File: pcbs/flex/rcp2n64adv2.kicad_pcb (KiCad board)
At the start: 2 copper layers, 129.6 x 25 mm, 17 parts, among them J1 Conn_01x01, J2 Conn_01x01, J3 Conn_01x01, J3.1 Conn_01x01, J4 Conn_01x01, J5 Conn_01x01, J6 Conn_01x30, U1 74LVC1G17, X1 n64_rcp_vid_aud_out_no_3v3_con, X2 Conn_01x01

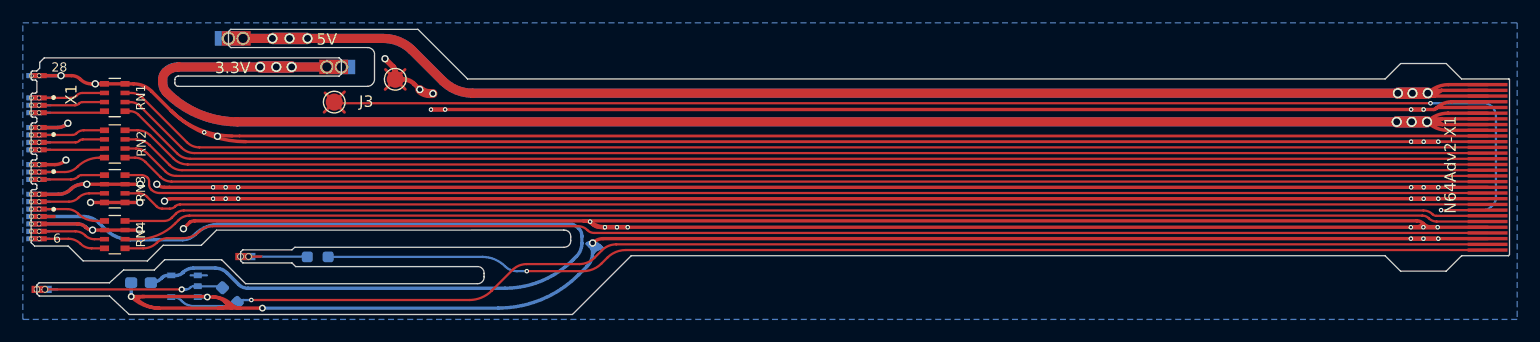
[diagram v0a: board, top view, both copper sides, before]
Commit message: update flex PCB with minor changes, e.g. added a logo
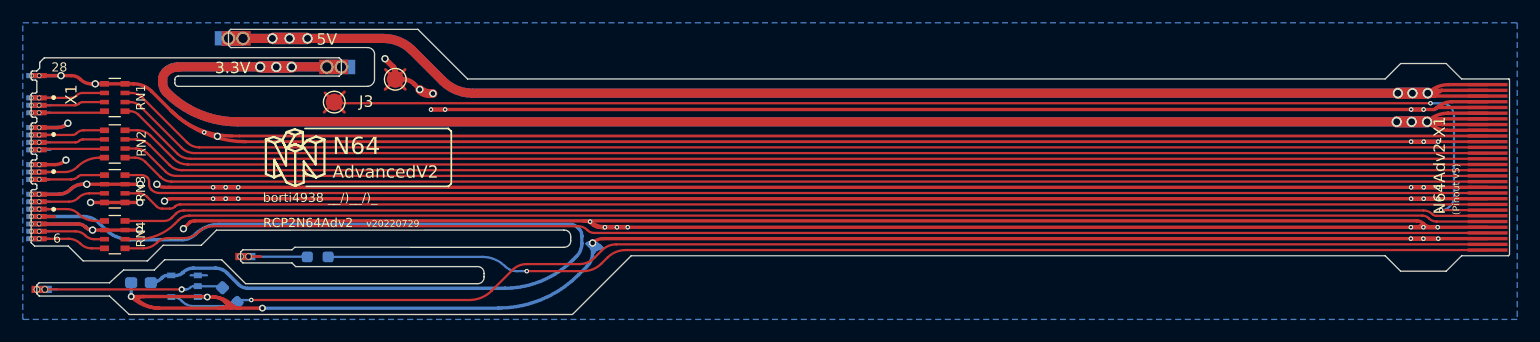
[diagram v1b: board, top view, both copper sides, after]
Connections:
- C1 pad 1: +3V3 -> VCC
- U1 pad 5: +3V3 -> VCC
- X2 pad 1: +3V3 -> VCC
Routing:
- net VCC: track 0.00 -> 91.3 mm
- net +3V3: track 381.2 -> 289.9 mm
- net Net-(J3-Pad1): track 124.1 -> 116.7 mm
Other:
- board text added: "(Pinout v5)"
- board text added: "(U1,C1) or R1"
- board text added: "AdvancedV2"
- board text added: "N64"
- board text added: "RCP2N64Adv2"
- board text added: "borti4938 __/)__/)_"
- board text added: "v20220729"

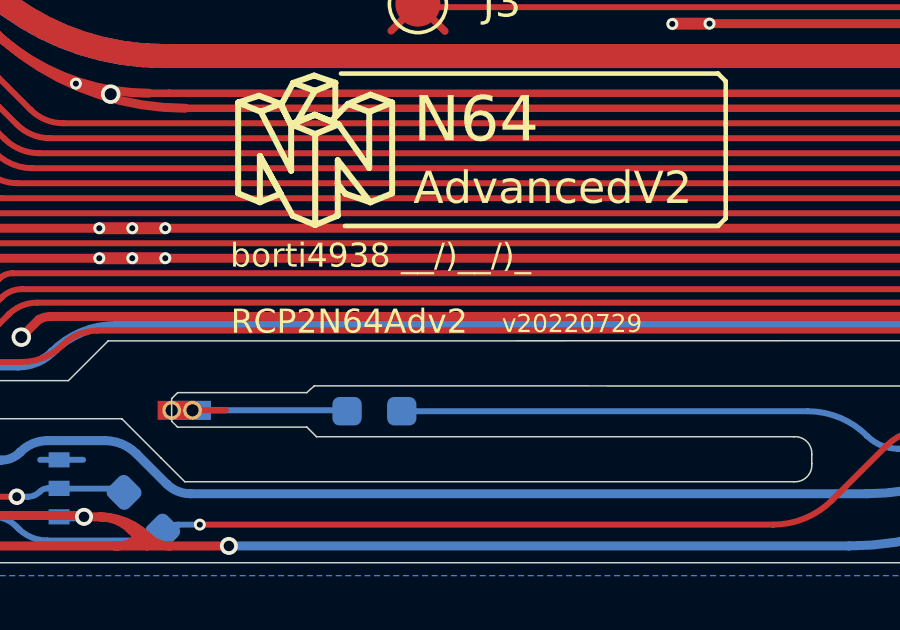
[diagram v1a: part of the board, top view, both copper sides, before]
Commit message: update main PCB with minor changes, e.g. ensure that solder mask bridges between 0.5mm pitched pads has min. 0.1mm thickness
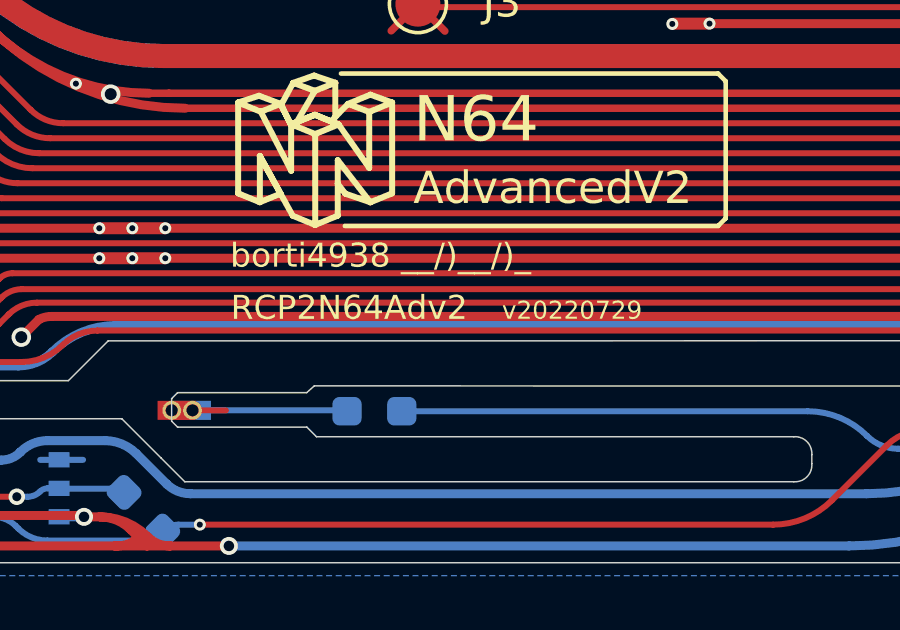
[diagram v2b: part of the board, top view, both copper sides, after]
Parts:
- C1: value C -> 100nF
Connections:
- net VCC renamed +3.3VA
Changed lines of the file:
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@@
   )
   (paper "A4")
+  (title_block
+    (title "RCP2N64Adv2")
+    (rev "v20220729")
+    (company "Peter 'borti4938' Bartmann")
+  )
   (layers
     (0 "F.Cu" signal)
@@
   )
   (net 0 "")
-  (net 1 "VCC")
+  (net 1 "+3.3VA")
   (net 2 "GND")
   (net 3 "+5V")
@@
     (fp_line (start 1.48 0) (end 1.92 0) (layer "Cmts.User") (width 0.12))
     (pad "1" smd rect (at 0.225 0) (size 1.35 0.45) (layers "B.Cu" "B.Mask")
-      (net 1 "VCC") (pinfunction "Pin_1") (pintype "passive"))
+      (net 1 "+3.3VA") (pinfunction "Pin_1") (pintype "passive"))
     (pad "1" thru_hole circle (at 0.675 0) (size 0.45 0.45) (drill 0.254) (layers *.Cu *.Mask)
-      (net 1 "VCC") (pinfunction "Pin_1") (pintype "passive"))
+      (net 1 "+3.3VA") (pinfunction "Pin_1") (pintype "passive"))
     (pad "1" smd rect (at 0.675 0) (size 1.35 0.45) (layers "F.Cu" "F.Mask")
-      (net 1 "VCC") (pinfunction "Pin_1") (pintype "passive"))
+      (net 1 "+3.3VA") (pinfunction "Pin_1") (pintype "passive"))
     (pad "1" thru_hole circle (at 0 0) (size 0.45 0.45) (drill 0.254) (layers *.Cu *.Mask)
-      (net 1 "VCC") (pinfunction "Pin_1") (pintype "passive"))
+      (net 1 "+3.3VA") (pinfunction "Pin_1") (pintype "passive"))
   )
   (footprint "smd_edge_con:large" (layer "F.Cu")
@@
       (effects (font (size 0.8 0.8) (thickness 0.15)) (justify mirror))
     )
-    (fp_text value "C" (at 0 -1.43) (layer "B.Fab")
+    (fp_text value "100nF" (at 0 -1.43) (layer "B.Fab")
       (effects (font (size 1 1) (thickness 0.15)) (justify mirror))
     )
@@
     (fp_line (start -0.8 -0.4) (end -0.8 0.4) (layer "B.Fab") (width 0.1))
     (pad "1" smd roundrect (at -0.8625 0 180) (size 1.075 0.95) (layers "B.Cu" "B.Paste" "B.Mask") (roundrect_rratio 0.25)
-      (net 1 "VCC") (pintype "passive"))
+      (net 1 "+3.3VA") (pintype "passive"))
     (pad "2" smd roundrect (at 0.8625 0 180) (size 1.075 0.95) (layers "B.Cu" "B.Paste" "B.Mask") (roundrect_rratio 0.25)
       (net 2 "GND") (pintype "passive"))
@@
       (net 19 "Net-(J6-Pad29)") (pintype "output"))
     (pad "5" smd rect (at 1.16 0.95 180) (size 0.7 0.51) (layers "B.Cu" "B.Paste" "B.Mask")
-      (net 1 "VCC") (pinfunction "VCC") (pintype "power_in"))
+      (net 1 "+3.3VA") (pinfunction "VCC") (pintype "power_in"))
     (model "${KICAD6_3DMODEL_DIR}/Package_SO.3dshapes/TSOP-5_1.65x3.05mm_P0.95mm.wrl"
       (offset (xyz 0 0 0))
@@
     (effects (font (size 1.0795 1.0795) (thickness 0.1905)) (justify left bottom))
   )
-  (gr_text "RCP2N64Adv2" (at 106.06 106.53) (layer "F.SilkS")
+  (gr_text "RCP2N64Adv2" (at 106.06 106.07) (layer "F.SilkS")
     (effects (font (size 0.8 0.8) (thickness 0.15)) (justify left))
   )
@@
     (effects (font (size 1 1) (thickness 0.15)))
   )
-  (gr_text "v20220729" (at 115.1 106.6) (layer "F.SilkS")
+  (gr_text "v20220729" (at 115.1 106.16) (layer "F.SilkS")
     (effects (font (size 0.6 0.6) (thickness 0.15)) (justify left))
   )

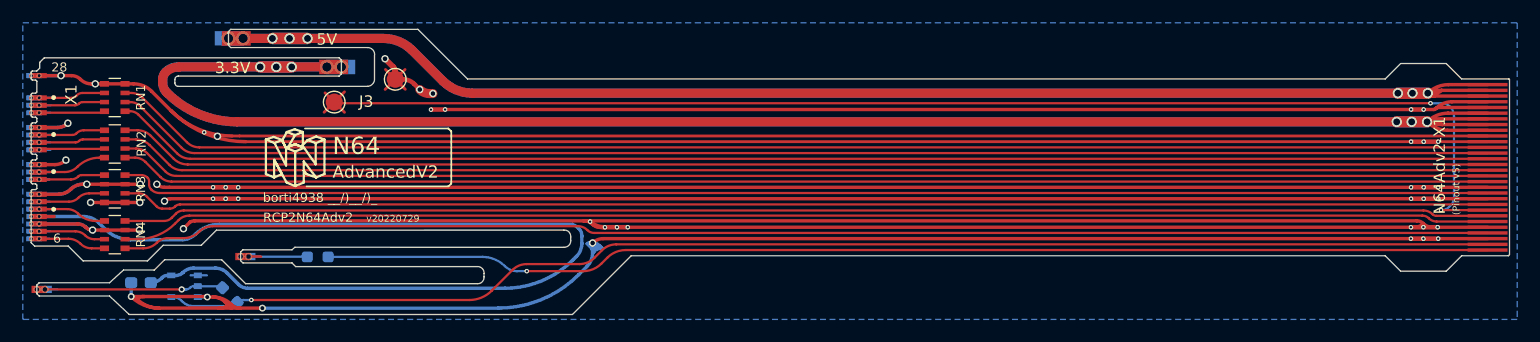
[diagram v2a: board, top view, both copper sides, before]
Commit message: update flex PCB: - add a feedback path for VI-Deblur - optimize implementation around U1 - add logo and license text to silkscreen
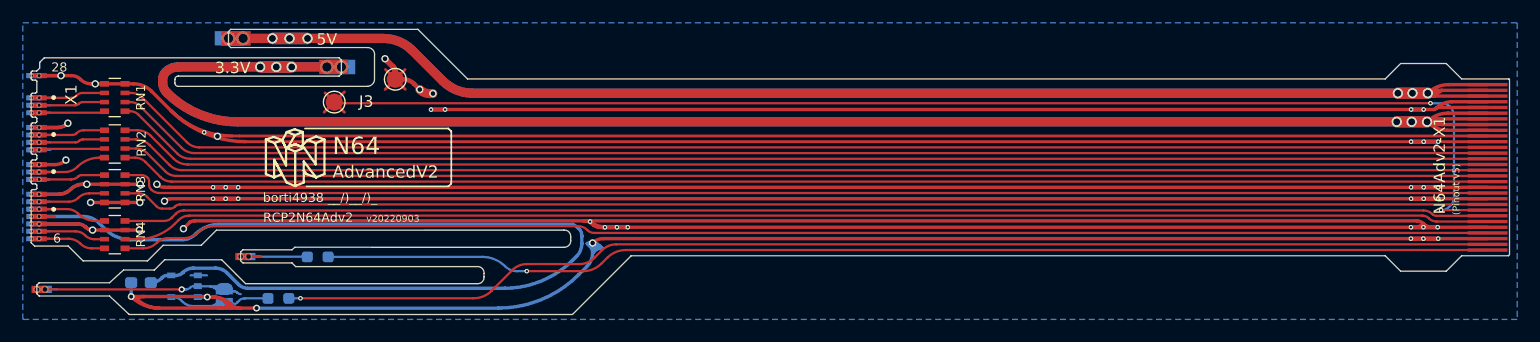
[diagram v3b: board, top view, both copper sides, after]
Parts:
- added REF**: OSHW-Logo_5.7x6mm_SilkScreen, Symbol:OSHW-Logo_5.7x6mm_SilkScreen, B.Cu at (111.3, 100.4)
- added SJ1: SolderJumper_2_Open, Jumper:SolderJumper-2_P1.3mm_Open_RoundedPad1.0x1.5mm, B.Cu at (102.7, 113.0)
- moved R1 4.27 mm to (107.4, 113.2), turned to 0 degrees
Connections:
- R1 pad 1: Net-(J4-Pad1) -> Net-(R1-Pad1)
- U1 pad 4: Net-(J6-Pad29) -> Net-(R1-Pad1)
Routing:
- net Net-(J6-Pad29): track 117.4 -> 106.7 mm
- net Net-(R1-Pad1): track 0.00 -> 8.88 mm
- net Net-(J4-Pad1): track 17.3 -> 19.0 mm
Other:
- board text added: "(U1,C1) or SJ1"
- board text added: "Licensed under CERN-OHL-W v2"
- board text added: "v20220903"
- board text removed: "(U1,C1) or R1"
- board text removed: "v20220729"

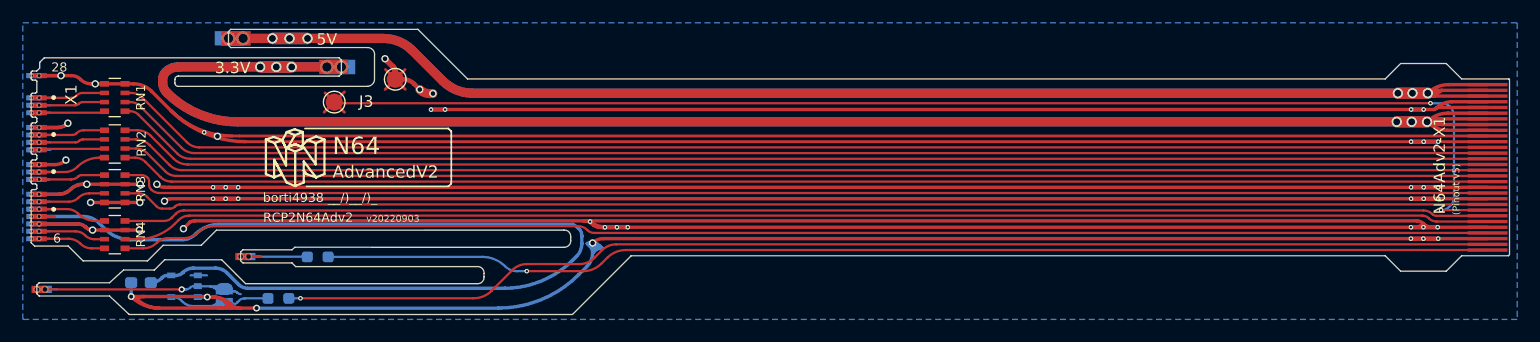
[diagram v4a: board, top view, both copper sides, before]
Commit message: Update flex-PCB: - move buffer IC to resistor array area of PCB (not on arms anymore) - add pads as backup if arms get ripped off
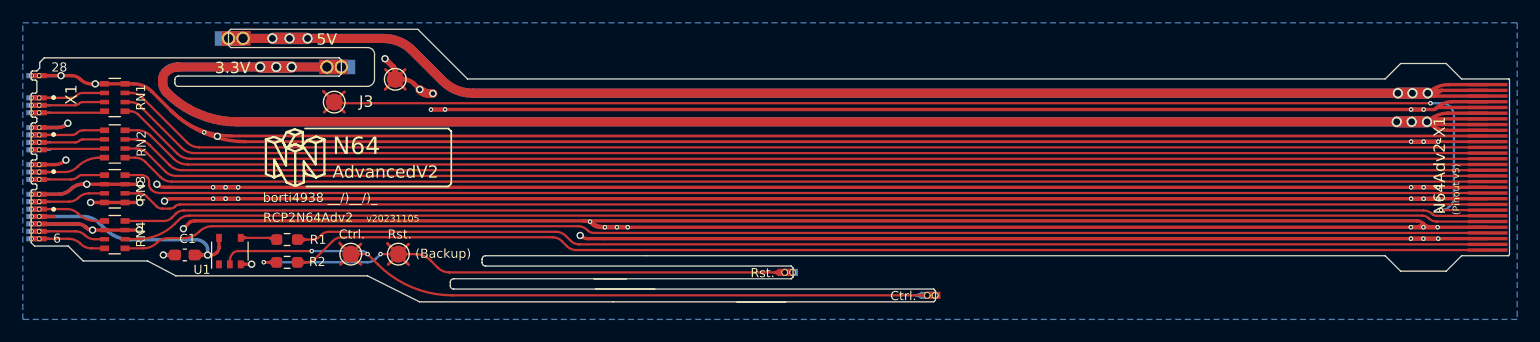
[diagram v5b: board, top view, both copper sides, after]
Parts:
- removed SJ1: SolderJumper_2_Open, Jumper:SolderJumper-2_P1.3mm_Open_RoundedPad1.0x1.5mm
- added J4.1: Conn_01x01, TestPoint:TestPoint_Pad_D1.5mm, F.Cu at (113.8, 109.3)
- added J5.1: Conn_01x01, TestPoint:TestPoint_Pad_D1.5mm, F.Cu at (117.9, 109.3)
- C1, J5, R1, R2, U1: moved to F.Cu
- moved J4 78.7 mm to (165.0, 112.9), turned to 180 degrees
- moved J5 48.4 mm to (152.5, 110.9), turned to 180 degrees
- moved R1 5.22 mm to (108.2, 108.0)
- moved U1 5.02 mm to (103.2, 109.0), turned to 90 degrees
- moved C1 4.54 mm to (99.2, 109.3)
- moved R2 2.72 mm to (108.2, 110.0)
- moved REF** 0.12 mm to (111.3, 100.5)
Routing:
- net +3.3VA: track 91.3 -> 21.0 mm, vias 0 -> 1
- net GND: track 983.5 -> 921.0 mm, vias 51 -> 50
- net Net-(J4-Pad1): track 19.0 -> 71.0 mm, vias 1 -> 2
- net Net-(J5-Pad1): track 6.29 -> 53.8 mm, vias 0 -> 2
- net Net-(R1-Pad1): track 8.88 -> 3.20 mm
- net Net-(J6-Pad30): track 102.5 -> 105.5 mm, vias 1 -> 0
- net Net-(J6-Pad29): track 106.7 -> 104.9 mm, vias 1 -> 0
- net (no net): track 1.43 -> 0.00 mm
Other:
- board size 129.6 x 25 mm -> 129.6 x 23.9 mm
- board text added: "(Backup)"
- board text added: "Ctrl."
- board text added: "Rst."
- board text added: "v20231105"
- board text removed: "(U1,C1) or SJ1"
- board text removed: "v20220903"

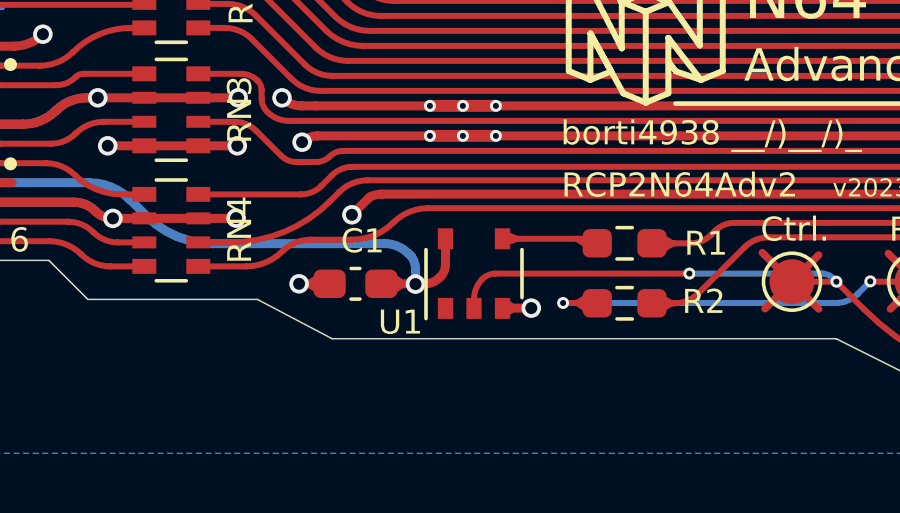
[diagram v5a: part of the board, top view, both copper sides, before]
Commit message: protect unconnected pad at U1 by small traces
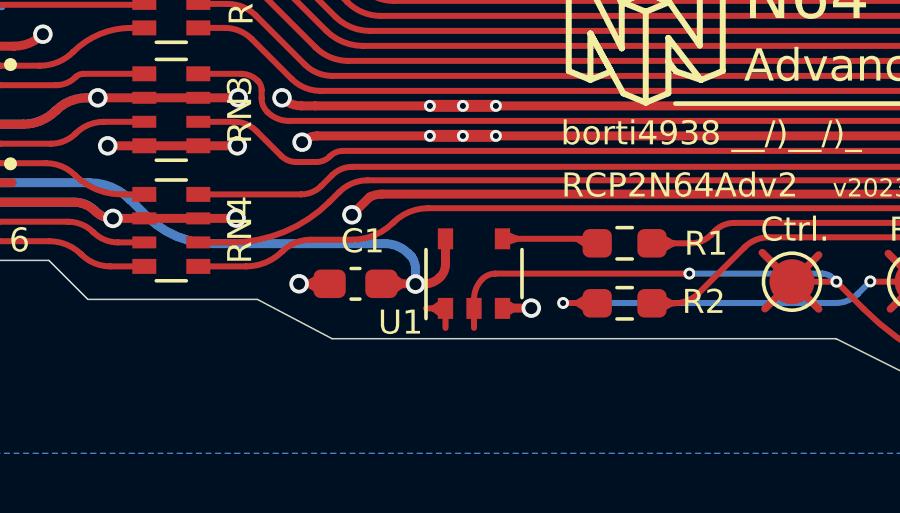
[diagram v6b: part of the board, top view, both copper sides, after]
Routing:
- net (no net): track 0.00 -> 1.31 mm
- net Net-(J4-Pad1): track 71.0 -> 71.7 mm
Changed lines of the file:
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@@
   (gr_line (start 104.52 110.16) (end 104.23 109.97) (layer "F.Cu") (width 0.2))
   (gr_line (start 163.76 112.89) (end 164.29 113.11) (layer "F.Cu") (width 0.2))
+  (gr_line (start 101.79 110.17) (end 102.09 109.96) (layer "F.Cu") (width 0.2))
   (gr_line (start 97.6 109.35) (end 97.97 109.59) (layer "F.Cu") (width 0.2))
   (gr_line (start 109.77 108) (end 109.43 107.8) (layer "F.Cu") (width 0.2))
   (gr_line (start 106.58 107.85) (end 106.98 108.12) (layer "F.Cu") (width 0.2))
   (gr_line (start 100.8 109.35) (end 100.42 109.63) (layer "F.Cu") (width 0.2))
+  (gr_line (start 101.79 110.17) (end 102.08 110.39) (layer "F.Cu") (width 0.2))
   (gr_line (start 106.58 109.99) (end 106.97 110.25) (layer "F.Cu") (width 0.2))
   (gr_line (start 104.59 107.85) (end 104.09 108.02) (layer "F.Cu") (width 0.2))
@@
     (effects (font (size 1.5113 1.5113) (thickness 0.2667)) (justify left bottom))
   )
+  (segment (start 102.2 110.16) (end 102.2 110.82) (width 0.2) (layer "F.Cu") (net 0))
+  (segment (start 102.2 110.17) (end 101.55 110.17) (width 0.2) (layer "F.Cu") (net 0))
   (segment (start 101.2 109.36) (end 101.19 109.35) (width 0.25) (layer "F.Cu") (net 1))
   (segment (start 86.435 105.98) (end 87.75 105.98) (width 0.3) (layer "F.Cu") (net 1))
@@
   (segment (start 115.23 109.28) (end 116.139563 110.189563) (width 0.2) (layer "F.Cu") (net 5))
   (segment (start 103.864558 109.01) (end 110.33 109.01) (width 0.2) (layer "F.Cu") (net 5))
+  (segment (start 103.15 110.204852) (end 103.15 110.82) (width 0.2) (layer "F.Cu") (net 5))
   (segment (start 113.74 109.29) (end 114.64 110.19) (width 0.25) (layer "F.Cu") (net 5))
   (segment (start 164.28 112.89) (end 122.658994 112.89) (width 0.2) (layer "F.Cu") (net 5))
